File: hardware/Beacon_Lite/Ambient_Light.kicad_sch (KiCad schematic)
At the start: 5 parts, among them J1 0805, U2 LTR-303ALS

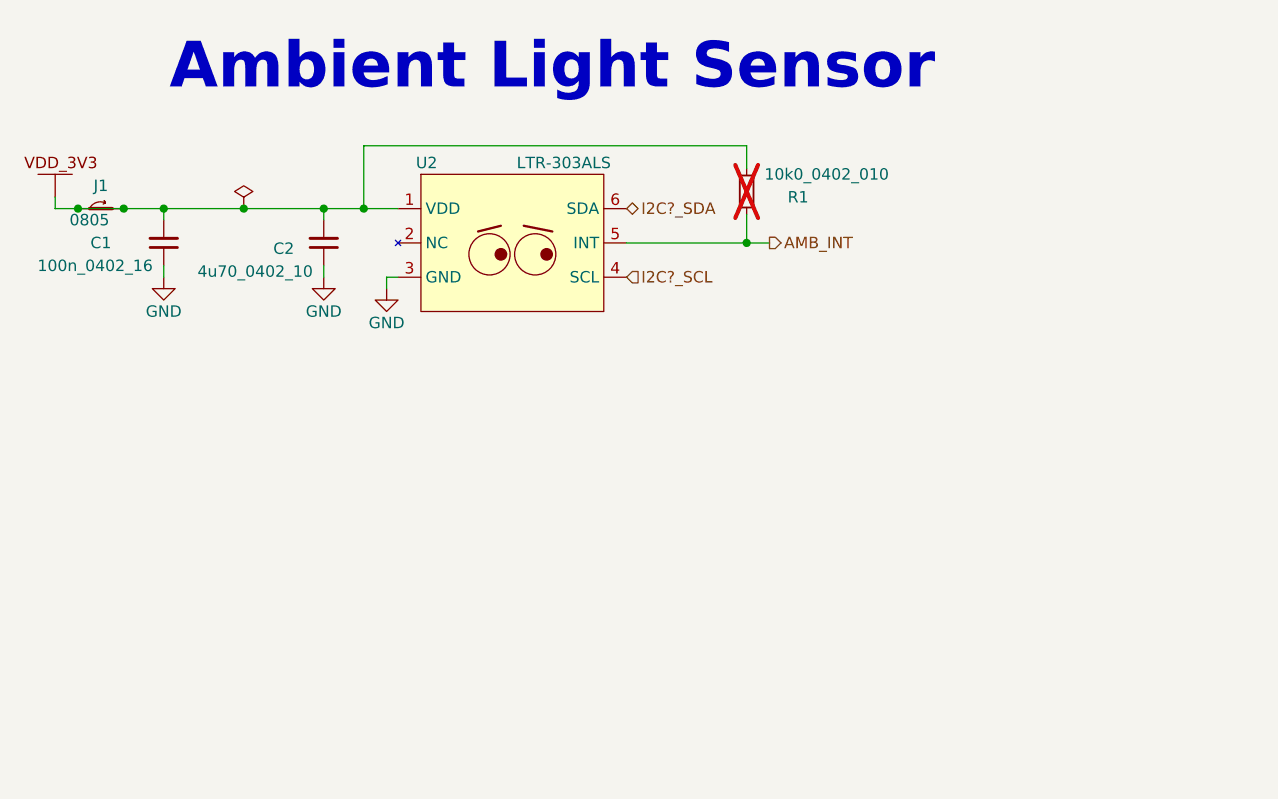
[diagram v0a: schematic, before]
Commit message: Started ST project. Create sch symbols.
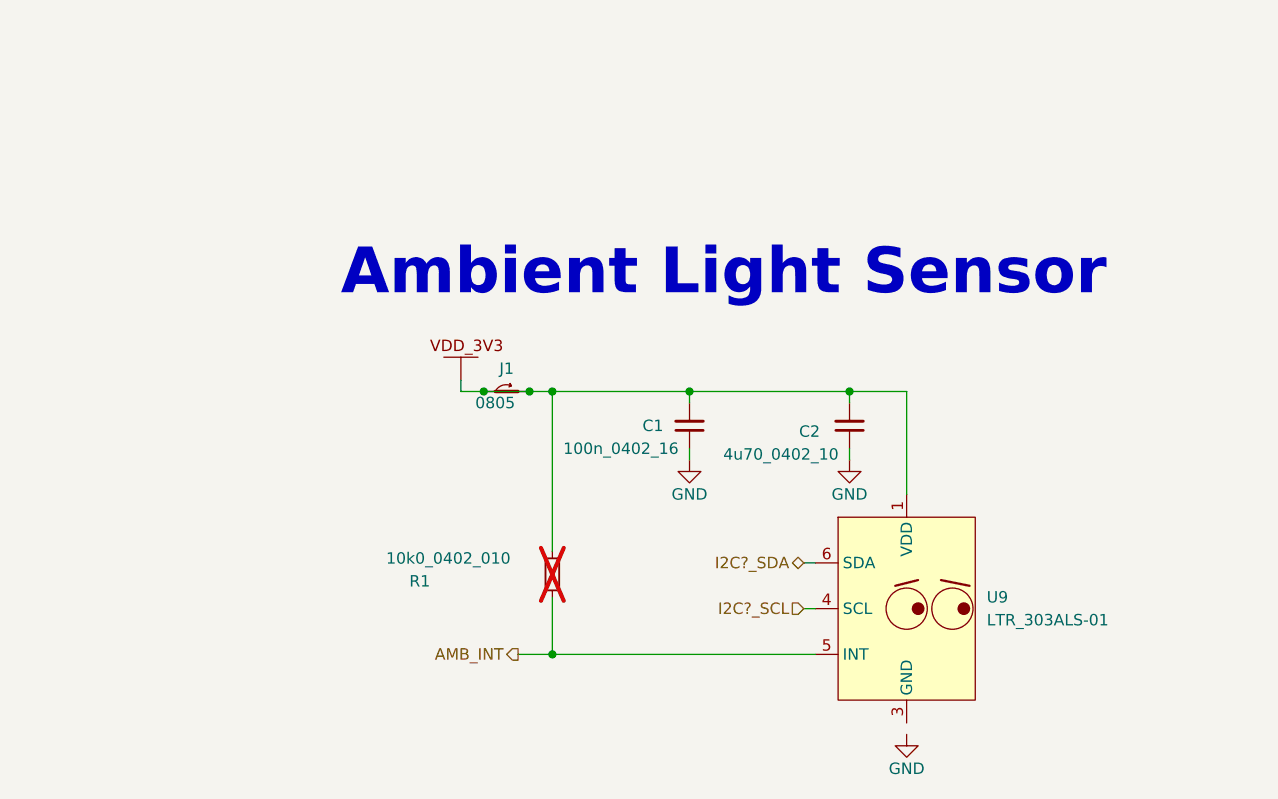
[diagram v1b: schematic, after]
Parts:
- removed U2: LTR-303ALS, Footprint_Library:LTR303ALS01, symbol Beacon_Library:LTR-303ALS
- added U9: LTR_303ALS-01, symbol Beacon_Lite_Library:LTR_303ALS-01
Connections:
- net AMB_INT: now also U9.5 (INT)
- net I2C?_SCL: now also U9.4 (SCL)
- net I2C?_SDA: now also U9.6 (SDA)
- net VDD_3V3: now also U9.1 (VDD)
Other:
- moved on the sheet: C1, C2, J1, R1

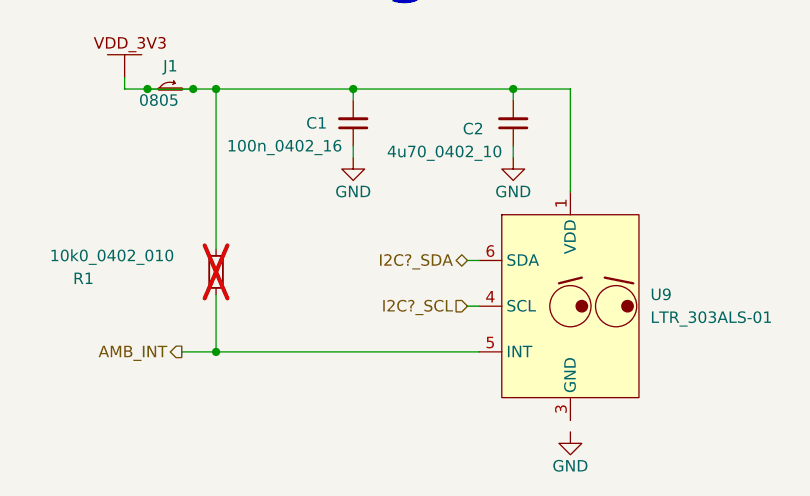
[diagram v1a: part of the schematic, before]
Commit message: Minor schematic and symbol updates
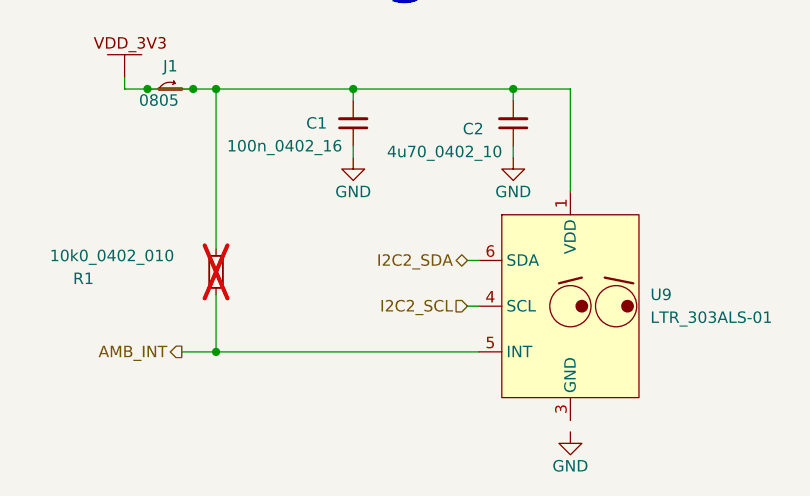
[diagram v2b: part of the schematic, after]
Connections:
- net I2C?_SCL renamed I2C2_SCL
- net I2C?_SDA renamed I2C2_SDA
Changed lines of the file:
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@@
 		)
 	)
-	(hierarchical_label "I2C?_SCL"
+	(hierarchical_label "I2C2_SCL"
 		(shape input)
 		(at 160.02 104.14 180)
@@
 		)
 		(property "Intersheetrefs" "${INTERSHEET_REFS}"
-			(at 149.1492 104.14 0)
+			(at 149.0283 104.14 0)
 			(effects
 				(font
@@
 		)
 	)
-	(hierarchical_label "I2C?_SDA"
+	(hierarchical_label "I2C2_SDA"
 		(shape bidirectional)
 		(at 160.02 99.06 180)
@@
 		)
 		(property "Intersheetrefs" "${INTERSHEET_REFS}"
-			(at 149.0887 99.06 0)
+			(at 148.9678 99.06 0)
 			(effects
 				(font

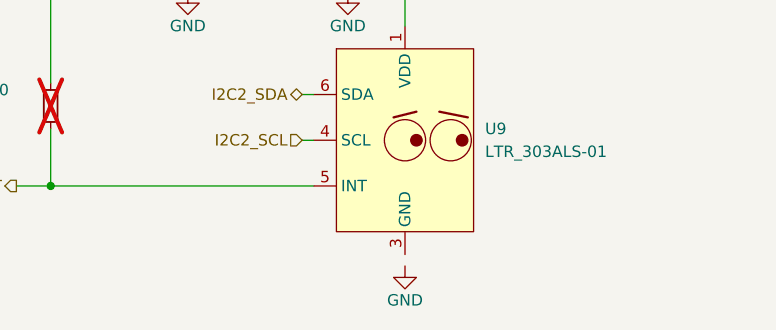
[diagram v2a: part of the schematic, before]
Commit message: Started programming NUCLEO-H533 in VSCODE
* Able to use C++ and C
* Successful able to debug
* Can blink an LED when button is pressed via an interrupt.
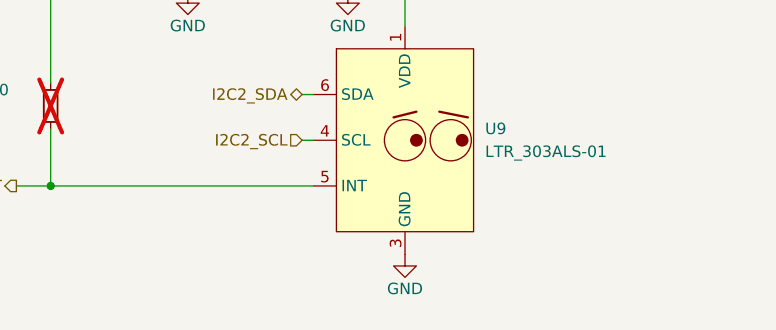
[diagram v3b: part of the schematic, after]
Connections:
- net GND: now also U9.3 (GND)
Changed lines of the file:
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@@
 	(symbol
 		(lib_id "power:GND")
-		(at 171.45 118.11 0)
+		(at 171.45 116.84 0)
 		(unit 1)
 		(exclude_from_sim no)
@@
 		(dnp no)
 		(property "Reference" "#PWR022"
-			(at 171.45 124.46 0)
+			(at 171.45 123.19 0)
 			(effects
 				(font
@@
 		)
 		(property "Value" "GND"
-			(at 171.45 121.92 0)
+			(at 171.45 120.65 0)
 			(effects
 				(font
@@
 		)
 		(property "Footprint" ""
-			(at 171.45 118.11 0)
+			(at 171.45 116.84 0)
 			(effects
 				(font
@@
 		)
 		(property "Datasheet" ""
-			(at 171.45 118.11 0)
+			(at 171.45 116.84 0)
 			(effects
 				(font
@@
 		)
 		(property "Description" ""
-			(at 171.45 118.11 0)
+			(at 171.45 116.84 0)
 			(effects
 				(font
